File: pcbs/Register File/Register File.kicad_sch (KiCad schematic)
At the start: 0 parts

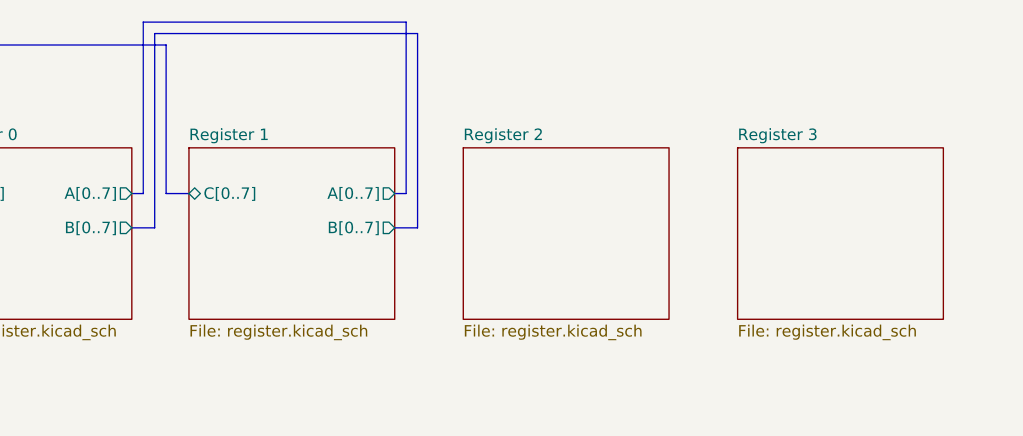
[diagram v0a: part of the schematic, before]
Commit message: More routing and connecting
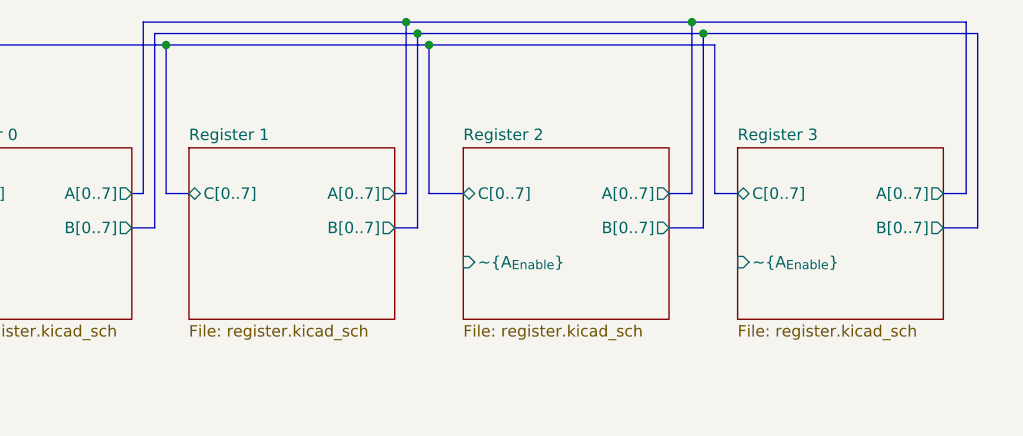
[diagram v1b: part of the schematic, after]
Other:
- sheet Register 2 ports: added A[0..7], B[0..7], C[0..7], ~{A_{Enable}}; removed none
- sheet Register 3 ports: added A[0..7], B[0..7], C[0..7], ~{A_{Enable}}; removed none
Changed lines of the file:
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@@
 (kicad_sch (version 20230121) (generator eeschema)
   (paper "A4")
+  (junction (at 115.57 40.64) (diameter 0) (color 0 0 0 0)
+  )
+  (junction (at 175.26 39.37) (diameter 0) (color 0 0 0 0)
+  )
+  (junction (at 144.78 40.64) (diameter 0) (color 0 0 0 0)
+  )
+  (junction (at 173.99 38.1) (diameter 0) (color 0 0 0 0)
+  )
+  (junction (at 143.51 39.37) (diameter 0) (color 0 0 0 0)
+  )
+  (junction (at 142.24 38.1) (diameter 0) (color 0 0 0 0)
+  )
   (bus (pts (xy 111.76 57.15) (xy 113.03 57.15))
     (stroke (width 0) (type default))
   )
+  (bus (pts (xy 175.26 60.96) (xy 171.45 60.96))
+    (stroke (width 0) (type default))
+  )
   (bus (pts (xy 115.57 40.64) (xy 87.63 40.64))
     (stroke (width 0) (type default))
@@
     (stroke (width 0) (type default))
   )
+  (bus (pts (xy 175.26 39.37) (xy 175.26 60.96))
+    (stroke (width 0) (type default))
+  )
   (bus (pts (xy 87.63 57.15) (xy 90.17 57.15))
     (stroke (width 0) (type default))
   )
+  (bus (pts (xy 176.53 40.64) (xy 176.53 57.15))
+    (stroke (width 0) (type default))
+  )
   (bus (pts (xy 142.24 38.1) (xy 142.24 57.15))
     (stroke (width 0) (type default))
   )
+  (bus (pts (xy 204.47 57.15) (xy 201.93 57.15))
+    (stroke (width 0) (type default))
+  )
   (bus (pts (xy 111.76 60.96) (xy 114.3 60.96))
     (stroke (width 0) (type default))
   )
+  (bus (pts (xy 205.74 39.37) (xy 205.74 60.96))
+    (stroke (width 0) (type default))
+  )
   (bus (pts (xy 114.3 39.37) (xy 143.51 39.37))
     (stroke (width 0) (type default))
@@
     (stroke (width 0) (type default))
   )
+  (bus (pts (xy 144.78 40.64) (xy 144.78 57.15))
+    (stroke (width 0) (type default))
+  )
   (bus (pts (xy 87.63 40.64) (xy 87.63 57.15))
     (stroke (width 0) (type default))
   )
+  (bus (pts (xy 115.57 40.64) (xy 144.78 40.64))
+    (stroke (width 0) (type default))
+  )
   (bus (pts (xy 115.57 57.15) (xy 115.57 40.64))
     (stroke (width 0) (type default))
@@
     (stroke (width 0) (type default))
   )
+  (bus (pts (xy 176.53 57.15) (xy 179.07 57.15))
+    (stroke (width 0) (type default))
+  )
   (bus (pts (xy 114.3 60.96) (xy 114.3 39.37))
     (stroke (width 0) (type default))
   )
+  (bus (pts (xy 144.78 40.64) (xy 176.53 40.64))
+    (stroke (width 0) (type default))
+  )
   (bus (pts (xy 143.51 60.96) (xy 140.97 60.96))
     (stroke (width 0) (type default))
   )
+  (bus (pts (xy 173.99 57.15) (xy 173.99 38.1))
+    (stroke (width 0) (type default))
+  )
+  (bus (pts (xy 144.78 57.15) (xy 148.59 57.15))
+    (stroke (width 0) (type default))
+  )
+  (bus (pts (xy 205.74 60.96) (xy 201.93 60.96))
+    (stroke (width 0) (type default))
+  )
+  (bus (pts (xy 204.47 38.1) (xy 204.47 57.15))
+    (stroke (width 0) (type default))
+  )
+  (bus (pts (xy 175.26 39.37) (xy 205.74 39.37))
+    (stroke (width 0) (type default))
+  )
+  (bus (pts (xy 143.51 39.37) (xy 175.26 39.37))
+    (stroke (width 0) (type default))
+  )
   (bus (pts (xy 142.24 57.15) (xy 140.97 57.15))
     (stroke (width 0) (type default))
   )
+  (bus (pts (xy 173.99 38.1) (xy 204.47 38.1))
+    (stroke (width 0) (type default))
+  )
+  (bus (pts (xy 173.99 38.1) (xy 142.24 38.1))
+    (stroke (width 0) (type default))
+  )
+  (bus (pts (xy 171.45 57.15) (xy 173.99 57.15))
+    (stroke (width 0) (type default))
+  )
   (sheet (at 148.59 52.07) (size 22.86 19.05) (fields_autoplaced)
     (stroke (width 0.1524) (type solid))
@@
       (effects (font (size 1.27 1.27)) (justify left top))
     )
+    (pin "B[0..7]" output (at 171.45 60.96 0)
+      (effects (font (size 1.27 1.27)) (justify right))
+    )
+    (pin "C[0..7]" bidirectional (at 148.59 57.15 180)
+      (effects (font (size 1.27 1.27)) (justify left))
+    )
+    (pin "~{A_{Enable}}" input (at 148.59 64.77 180)
+      (effects (font (size 1.27 1.27)) (justify left))
+    )
+    (pin "A[0..7]" output (at 171.45 57.15 0)
+      (effects (font (size 1.27 1.27)) (justify right))
+    )
     (instances
       (project "Register File"
@@
       (effects (font (size 1.27 1.27)) (justify left top))
     )
-    (instances
+    (pin "B[0..7]" output (at 201.93 60.96 0)
+      (effects (font (size 1.27 1.27)) (justify right))
+    )
+    (pin "C[0..7]" bidirectional (at 179.07 57.15 180)
+      (effects (font (size 1.27 1.27)) (justify left))
+    )
+    (pin "~{A_{Enable}}" input (at 179.07 64.77 180)
+      (effects (font (size 1.27 1.27)) (justify left))
+    )
+    (pin "A[0..7]" output (at 201.93 57.15 0)
+      (effects (font (size 1.27 1.27)) (justify right))
+    )
+    (instances

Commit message: More work
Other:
- sheet Register 4 ports: added A[0..7], B[0..7], C[0..7], ~{A_{Enable}}; removed none

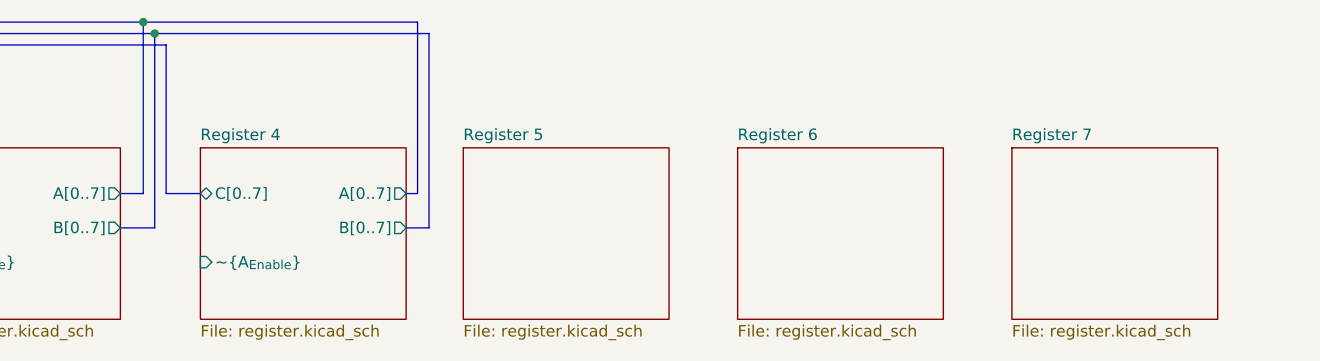
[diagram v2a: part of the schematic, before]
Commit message: Fixing ordering of registers in schematic
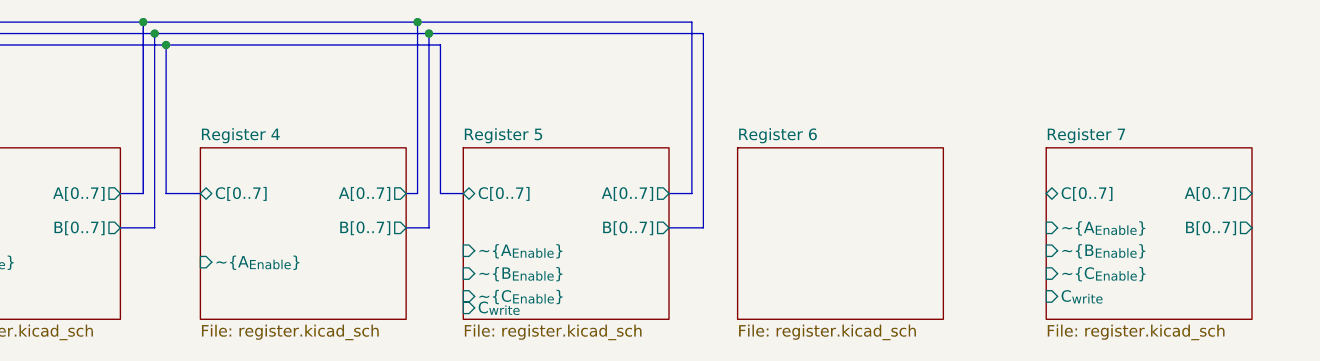
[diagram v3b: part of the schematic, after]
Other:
- sheet Register 5 ports: added A[0..7], B[0..7], C[0..7], C_{write}, ~{A_{Enable}}, ~{B_{Enable}}, ~{C_{Enable}}; removed none
- sheet Register 7 ports: added A[0..7], B[0..7], C[0..7], C_{write}, ~{A_{Enable}}, ~{B_{Enable}}, ~{C_{Enable}}; removed none
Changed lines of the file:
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@@
   (junction (at 105.41 40.64) (diameter 0) (color 0 0 0 0)
   )
+  (junction (at 166.37 40.64) (diameter 0) (color 0 0 0 0)
+  )
   (junction (at 74.93 41.91) (diameter 0) (color 0 0 0 0)
   )
@@
   (junction (at 73.66 40.64) (diameter 0) (color 0 0 0 0)
   )
+  (junction (at 165.1 39.37) (diameter 0) (color 0 0 0 0)
+  )
   (junction (at 134.62 39.37) (diameter 0) (color 0 0 0 0)
   )
+  (junction (at 137.16 41.91) (diameter 0) (color 0 0 0 0)
+  )
   (junction (at 106.68 41.91) (diameter 0) (color 0 0 0 0)
   )
   (junction (at 72.39 39.37) (diameter 0) (color 0 0 0 0)
   )
+  (bus (pts (xy 167.64 58.42) (xy 170.18 58.42))
+    (stroke (width 0) (type default))
+  )
   (bus (pts (xy 41.91 58.42) (xy 43.18 58.42))
     (stroke (width 0) (type default))
@@
     (stroke (width 0) (type default))
   )
+  (bus (pts (xy 196.85 40.64) (xy 166.37 40.64))
+    (stroke (width 0) (type default))
+  )
   (bus (pts (xy 165.1 39.37) (xy 165.1 58.42))
     (stroke (width 0) (type default))
   )
+  (bus (pts (xy 195.58 39.37) (xy 195.58 58.42))
+    (stroke (width 0) (type default))
+  )
   (bus (pts (xy 17.78 41.91) (xy 17.78 58.42))
     (stroke (width 0) (type default))
@@
     (stroke (width 0) (type default))
   )
+  (bus (pts (xy 167.64 41.91) (xy 167.64 58.42))
+    (stroke (width 0) (type default))
+  )
+  (bus (pts (xy 165.1 39.37) (xy 195.58 39.37))
+    (stroke (width 0) (type default))
+  )
   (bus (pts (xy 134.62 39.37) (xy 165.1 39.37))
     (stroke (width 0) (type default))
@@
     (stroke (width 0) (type default))
   )
+  (bus (pts (xy 193.04 62.23) (xy 196.85 62.23))
+    (stroke (width 0) (type default))
+  )
   (bus (pts (xy 106.68 58.42) (xy 109.22 58.42))
     (stroke (width 0) (type default))
   )
+  (bus (pts (xy 137.16 41.91) (xy 167.64 41.91))
+    (stroke (width 0) (type default))
+  )
   (bus (pts (xy 44.45 62.23) (xy 44.45 40.64))
     (stroke (width 0) (type default))
@@
   )
   (bus (pts (xy 104.14 39.37) (xy 72.39 39.37))
+    (stroke (width 0) (type default))
+  )
+  (bus (pts (xy 196.85 62.23) (xy 196.85 40.64))
+    (stroke (width 0) (type default))
+  )
+  (bus (pts (xy 195.58 58.42) (xy 193.04 58.42))
     (stroke (width 0) (type default))
   )
@@
     )
   )
-  (sheet (at 170.18 53.34) (size 22.86 19.05) (fields_autoplaced)
-    (stroke (width 0.1524) (type solid))
-    (fill (color 0 0 0 0.0000))
-    (property "Sheetname" "Register 5" (at 170.18 52.6284 0)
-      (effects (font (size 1.27 1.27)) (justify left bottom))
-    )
-    (property "Sheetfile" "register.kicad_sch" (at 170.18 72.9746 0)
-      (effects (font (size 1.27 1.27)) (justify left top))
+  (sheet (at 234.95 53.34) (size 22.86 19.05) (fields_autoplaced)
+    (stroke (width 0.1524) (type solid))
+    (fill (color 0 0 0 0.0000))
+    (property "Sheetname" "Register 7" (at 234.95 52.6284 0)
+      (effects (font (size 1.27 1.27)) (justify left bottom))
+    )
+    (property "Sheetfile" "register.kicad_sch" (at 234.95 72.9746 0)
+      (effects (font (size 1.27 1.27)) (justify left top))
+    )
+    (pin "C_{write}" input (at 234.95 69.85 180)
+      (effects (font (size 1.27 1.27)) (justify left))
+    )
+    (pin "C[0..7]" bidirectional (at 234.95 58.42 180)
+      (effects (font (size 1.27 1.27)) (justify left))
+    )
+    (pin "B[0..7]" output (at 257.81 62.23 0)
+      (effects (font (size 1.27 1.27)) (justify right))
+    )
+    (pin "~{B_{Enable}}" input (at 234.95 64.77 180)
+      (effects (font (size 1.27 1.27)) (justify left))
+    )
+    (pin "~{C_{Enable}}" input (at 234.95 67.31 180)
+      (effects (font (size 1.27 1.27)) (justify left))
+    )
+    (pin "~{A_{Enable}}" input (at 234.95 62.23 180)
+      (effects (font (size 1.27 1.27)) (justify left))
+    )
+    (pin "A[0..7]" output (at 257.81 58.42 0)
+      (effects (font (size 1.27 1.27)) (justify right))
     )
     (instances
@@
     )
   )
-  (sheet (at 231.14 53.34) (size 22.86 19.05) (fields_autoplaced)
-    (stroke (width 0.1524) (type solid))
-    (fill (color 0 0 0 0.0000))
-    (property "Sheetname" "Register 7" (at 231.14 52.6284 0)
-      (effects (font (size 1.27 1.27)) (justify left bottom))
-    )
-    (property "Sheetfile" "register.kicad_sch" (at 231.14 72.9746 0)
-      (effects (font (size 1.27 1.27)) (justify left top))
-    )
-    (instances
+  (sheet (at 170.18 53.34) (size 22.86 19.05) (fields_autoplaced)
+    (stroke (width 0.1524) (type solid))
+    (fill (color 0 0 0 0.0000))
+    (property "Sheetname" "Register 5" (at 170.18 52.6284 0)
+      (effects (font (size 1.27 1.27)) (justify left bottom))
+    )
+    (property "Sheetfile" "register.kicad_sch" (at 170.18 72.9746 0)
+      (effects (font (size 1.27 1.27)) (justify left top))
+    )
+    (pin "C_{write}" input (at 170.18 71.12 180)
+      (effects (font (size 1.27 1.27)) (justify left))
+    )
+    (pin "C[0..7]" bidirectional (at 170.18 58.42 180)
+      (effects (font (size 1.27 1.27)) (justify left))
+    )
+    (pin "B[0..7]" output (at 193.04 62.23 0)
+      (effects (font (size 1.27 1.27)) (justify right))
+    )
+    (pin "~{B_{Enable}}" input (at 170.18 67.31 180)
+      (effects (font (size 1.27 1.27)) (justify left))
+    )
+    (pin "~{C_{Enable}}" input (at 170.18 69.85 180)
+      (effects (font (size 1.27 1.27)) (justify left))
+    )
+    (pin "~{A_{Enable}}" input (at 170.18 64.77 180)
+      (effects (font (size 1.27 1.27)) (justify left))
+    )
+    (pin "A[0..7]" output (at 193.04 58.42 0)
+      (effects (font (size 1.27 1.27)) (justify right))
+    )
+    (instances

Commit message: Yet more routing
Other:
- added sheet Selectors (selectors.kicad_sch)
- sheet Register 0 ports: added C_{write}, ~{A_{Enable}}, ~{B_{Enable}}, ~{C_{Enable}}; removed none
- sheet Register 1 ports: added C_{write}, ~{A_{Enable}}, ~{B_{Enable}}, ~{C_{Enable}}; removed none
- sheet Register 6 ports: added A[0..7], B[0..7], C[0..7], C_{write}, ~{A_{Enable}}, ~{B_{Enable}}, ~{C_{Enable}}; removed none

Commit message: More work
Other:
- sheet Register 2 ports: added C_{write}, ~{B_{Enable}}, ~{C_{Enable}}; removed none
- sheet Register 3 ports: added C_{write}, ~{B_{Enable}}, ~{C_{Enable}}; removed none
- sheet Register 4 ports: added C_{write}, ~{B_{Enable}}, ~{C_{Enable}}; removed none
- sheet Selectors ports: added C_{Write}[0..7], R_{A}[0..2], R_{B}[0..2], R_{C}[0..2], ~{B_{select}}[0..7], ~{C_{select}}[0..7]; removed none

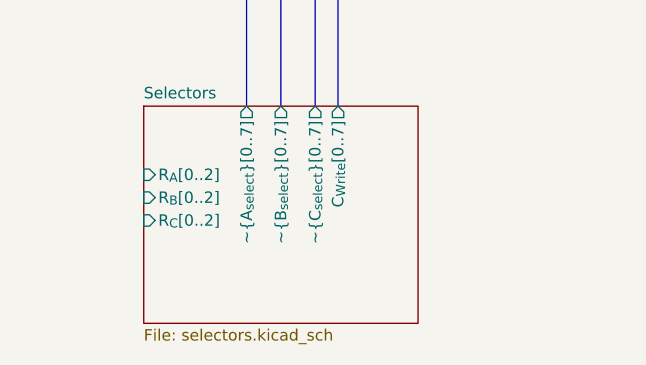
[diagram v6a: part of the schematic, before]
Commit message: More control logic
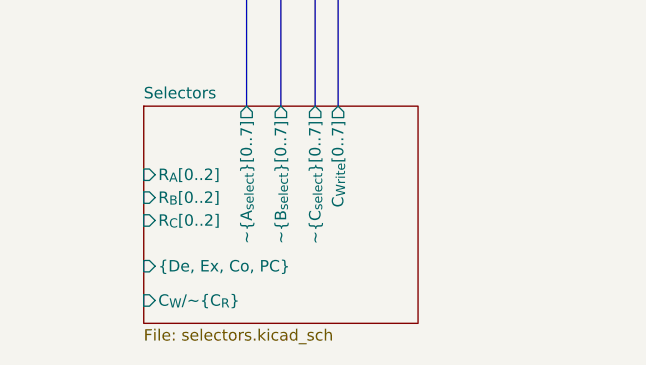
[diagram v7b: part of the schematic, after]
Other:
- sheet Selectors ports: added C_{W}/~{C_{R}}, {De, Ex, Co, PC}; removed none
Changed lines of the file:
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@@
       (effects (font (size 1.27 1.27)) (justify right))
+    )
+    (pin "C_{W}{slash}~{C_{R}}" input (at 31.75 166.37 180)
+      (effects (font (size 1.27 1.27)) (justify left))
+    )
+    (pin "{De, Ex, Co, PC}" input (at 31.75 162.56 180)
+      (effects (font (size 1.27 1.27)) (justify left))
     )
     (instances

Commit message: Routing the connector Pt 1 of n
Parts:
- added J101: Conn_02x20_Odd_Even, Connector_PinHeader_2.54mm:PinHeader_2x20_P2.54mm_Vertical, symbol Connector_Generic:Conn_02x20_Odd_Even
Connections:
- net Selectors/C_{W}/~{C_{R}}: now also J101.2 (Pin_2)
- new net +5V: J101.40 (Pin_40)
- new net A0: J101.4 (Pin_4)
- new net A1: J101.6 (Pin_6)
- new net A2: J101.8 (Pin_8)
- new net A3: J101.10 (Pin_10)
- new net A4: J101.12 (Pin_12)
- new net A5: J101.14 (Pin_14)
- new net A6: J101.16 (Pin_16)
- new net A7: J101.18 (Pin_18)
- new net B0: J101.24 (Pin_24)
- new net B1: J101.26 (Pin_26)
- new net B2: J101.28 (Pin_28)
- new net B3: J101.30 (Pin_30)
- new net B4: J101.32 (Pin_32)
- new net B5: J101.34 (Pin_34)
- new net B6: J101.36 (Pin_36)
- new net B7: J101.38 (Pin_38)
- new net C0: J101.23 (Pin_23)
- new net C1: J101.25 (Pin_25)
- new net C2: J101.27 (Pin_27)
- new net C3: J101.29 (Pin_29)
- new net C4: J101.31 (Pin_31)
- new net C5: J101.33 (Pin_33)
- new net C6: J101.35 (Pin_35)
- new net C7: J101.37 (Pin_37)
- new net Co: J101.20 (Pin_20)
- new net De: J101.19 (Pin_19)
- new net Ex: J101.21 (Pin_21)
- new net GND: J101.39 (Pin_39)
- new net PC: J101.22 (Pin_22)
- new net R_{A}0: J101.1 (Pin_1)
- new net R_{A}1: J101.3 (Pin_3)
- new net R_{A}2: J101.5 (Pin_5)
- new net R_{B}0: J101.7 (Pin_7)
- new net R_{B}1: J101.9 (Pin_9)
- new net R_{B}2: J101.11 (Pin_11)
- new net R_{C}0: J101.13 (Pin_13)
- new net R_{C}1: J101.15 (Pin_15)
- new net R_{C}2: J101.17 (Pin_17)
